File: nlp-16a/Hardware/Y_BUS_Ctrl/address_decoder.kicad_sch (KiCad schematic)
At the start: 20 parts, among them U41 CD74HC00, U42 CD74HC00

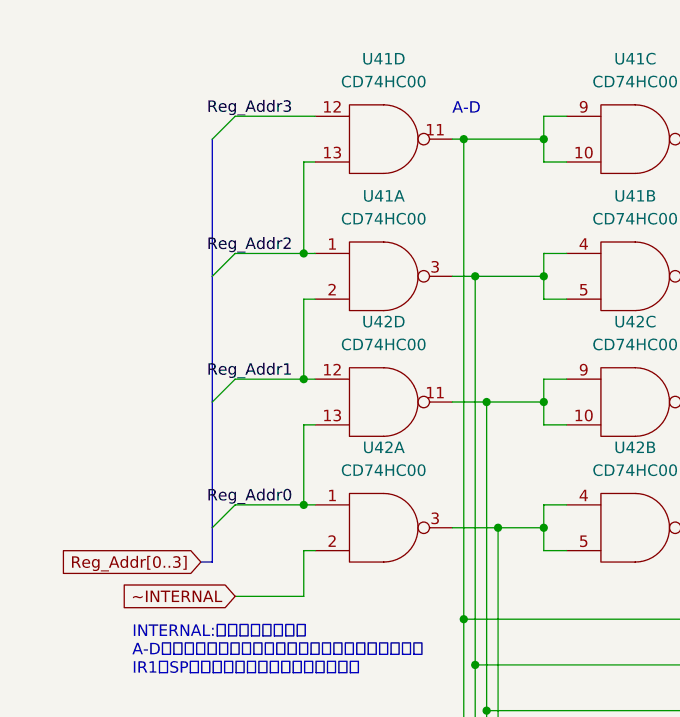
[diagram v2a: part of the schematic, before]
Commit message: Y BUS制御の基板をとりあえず描いた．ビアとかはまた後で
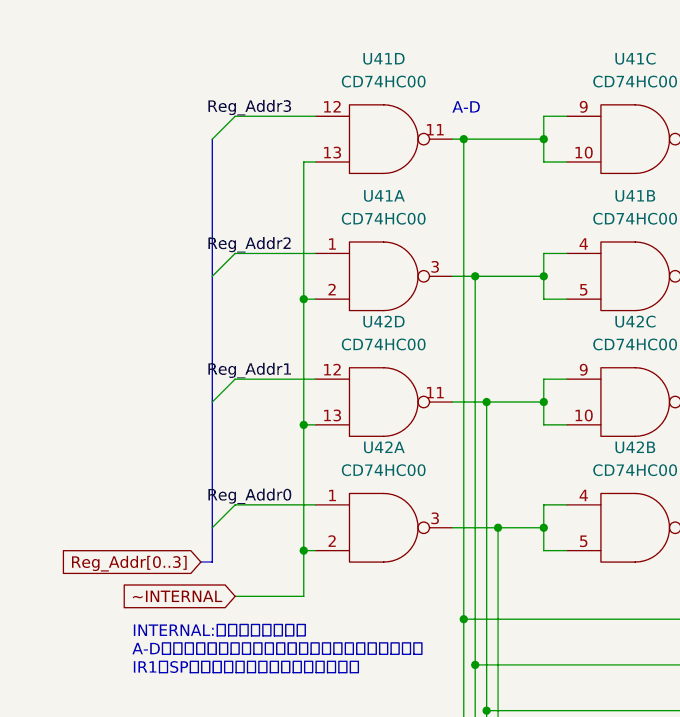
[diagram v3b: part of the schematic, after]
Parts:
- D17, D18, D19, D20, D21, D22, D23, D24, D25, D26, D27, D28, D29, D30, D31, D32: footprint (none) -> LED_THT:LED_D3.0mm
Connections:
- net Reg_Addr0: no longer U42.13
- net Reg_Addr1: no longer U41.2
- net Reg_Addr2: no longer U41.13
- net ~INTERNAL: now also U41.13, U41.2, U42.13
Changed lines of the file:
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@@
   (junction (at 142.24 83.82) (diameter 0) (color 0 0 0 0)
   )
+  (junction (at 34.29 68.58) (diameter 0) (color 0 0 0 0)
+  )
   (junction (at 115.57 114.3) (diameter 0) (color 0 0 0 0)
   )
@@
   (junction (at 252.73 48.26) (diameter 0) (color 0 0 0 0)
   )
-  (junction (at 34.29 49.53) (diameter 0) (color 0 0 0 0)
-  )
   (junction (at 172.72 157.48) (diameter 0) (color 0 0 0 0)
   )
@@
   (junction (at 256.54 81.28) (diameter 0) (color 0 0 0 0)
   )
-  (junction (at 34.29 35.56) (diameter 0) (color 0 0 0 0)
-  )
   (junction (at 161.29 78.74) (diameter 0) (color 0 0 0 0)
   )
@@
   (junction (at 60.96 66.04) (diameter 0) (color 0 0 0 0)
   )
-  (junction (at 34.29 63.5) (diameter 0) (color 0 0 0 0)
-  )
   (junction (at 252.73 142.24) (diameter 0) (color 0 0 0 0)
   )
@@
   (junction (at 276.86 41.91) (diameter 0) (color 0 0 0 0)
   )
+  (junction (at 34.29 40.64) (diameter 0) (color 0 0 0 0)
+  )
   (junction (at 55.88 91.44) (diameter 0) (color 0 0 0 0)
   )
@@
   (junction (at 82.55 88.9) (diameter 0) (color 0 0 0 0)
   )
+  (junction (at 34.29 54.61) (diameter 0) (color 0 0 0 0)
+  )
   (junction (at 229.87 142.24) (diameter 0) (color 0 0 0 0)
   )
@@
     (stroke (width 0) (type default) (color 0 0 0 0))
   )
-  (wire (pts (xy 34.29 35.56) (xy 35.56 35.56))
-    (stroke (width 0) (type default) (color 0 0 0 0))
-  )
   (wire (pts (xy 53.34 147.32) (xy 187.96 147.32))
     (stroke (width 0) (type default) (color 0 0 0 0))
@@
     (stroke (width 0) (type default) (color 0 0 0 0))
   )
-  (wire (pts (xy 34.29 54.61) (xy 34.29 63.5))
-    (stroke (width 0) (type default) (color 0 0 0 0))
-  )
   (wire (pts (xy 187.96 114.3) (xy 184.15 114.3))
     (stroke (width 0) (type default) (color 0 0 0 0))
@@
     (stroke (width 0) (type default) (color 0 0 0 0))
   )
+  (wire (pts (xy 34.29 40.64) (xy 34.29 54.61))
+    (stroke (width 0) (type default) (color 0 0 0 0))
+  )
   (wire (pts (xy 237.49 86.36) (xy 260.35 86.36))
     (stroke (width 0) (type default) (color 0 0 0 0))
@@
     (stroke (width 0) (type default) (color 0 0 0 0))
   )
+  (wire (pts (xy 34.29 25.4) (xy 34.29 40.64))
+    (stroke (width 0) (type default) (color 0 0 0 0))
+  )
   (wire (pts (xy 52.07 142.24) (xy 92.71 142.24))
     (stroke (width 0) (type default) (color 0 0 0 0))
@@
     (stroke (width 0) (type default) (color 0 0 0 0))
   )
-  (wire (pts (xy 34.29 49.53) (xy 35.56 49.53))
-    (stroke (width 0) (type default) (color 0 0 0 0))
-  )
   (wire (pts (xy 187.96 139.7) (xy 187.96 147.32))
     (stroke (width 0) (type default) (color 0 0 0 0))
@@
     (stroke (width 0) (type default) (color 0 0 0 0))
   )
-  (wire (pts (xy 34.29 25.4) (xy 34.29 35.56))
-    (stroke (width 0) (type default) (color 0 0 0 0))
-  )
-  (wire (pts (xy 26.67 63.5) (xy 34.29 63.5))
-    (stroke (width 0) (type default) (color 0 0 0 0))
-  )
   (wire (pts (xy 142.24 48.26) (xy 138.43 48.26))
     (stroke (width 0) (type default) (color 0 0 0 0))
@@
     (stroke (width 0) (type default) (color 0 0 0 0))
   )
-  (wire (pts (xy 34.29 63.5) (xy 35.56 63.5))
+  (wire (pts (xy 26.67 63.5) (xy 35.56 63.5))
     (stroke (width 0) (type default) (color 0 0 0 0))
   )
@@
     (stroke (width 0) (type default) (color 0 0 0 0))
   )
-  (wire (pts (xy 26.67 35.56) (xy 34.29 35.56))
+  (wire (pts (xy 26.67 35.56) (xy 35.56 35.56))
     (stroke (width 0) (type default) (color 0 0 0 0))
   )
@@
     (stroke (width 0) (type default) (color 0 0 0 0))
   )
+  (wire (pts (xy 34.29 54.61) (xy 34.29 68.58))
+    (stroke (width 0) (type default) (color 0 0 0 0))
+  )
   (wire (pts (xy 256.54 139.7) (xy 256.54 147.32))
     (stroke (width 0) (type default) (color 0 0 0 0))
@@
     (stroke (width 0) (type default) (color 0 0 0 0))
   )
-  (wire (pts (xy 34.29 40.64) (xy 34.29 49.53))
-    (stroke (width 0) (type default) (color 0 0 0 0))
-  )
   (wire (pts (xy 191.77 140.97) (xy 195.58 140.97))
     (stroke (width 0) (type default) (color 0 0 0 0))
@@
     (stroke (width 0) (type default) (color 0 0 0 0))
   )
-  (wire (pts (xy 26.67 49.53) (xy 34.29 49.53))
+  (wire (pts (xy 26.67 49.53) (xy 35.56 49.53))
     (stroke (width 0) (type default) (color 0 0 0 0))
   )
@@
     (property "Reference" "D29" (id 0) (at 193.04 116.84 0))
     (property "Value" "LED" (id 1) (at 189.23 116.84 0))
-    (property "Footprint" "" (id 2) (at 191.77 114.3 0)
+    (property "Footprint" "LED_THT:LED_D3.0mm" (id 2) (at 191.77 114.3 0)
       (effects (font (size 1.27 1.27)) hide)
     )
@@
     (property "Reference" "D26" (id 0) (at 124.46 116.84 0))
     (property "Value" "LED" (id 1) (at 120.65 116.84 0))
-    (property "Footprint" "" (id 2) (at 123.19 114.3 0)
+    (property "Footprint" "LED_THT:LED_D3.0mm" (id 2) (at 123.19 114.3 0)
       (effects (font (size 1.27 1.27)) hide)
     )
@@
     (property "Reference" "D22" (id 0) (at 215.9 50.8 0))
     (property "Value" "LED" (id 1) (at 212.09 50.8 0))
-    (property "Footprint" "" (id 2) (at 214.63 48.26 0)
+    (property "Footprint" "LED_THT:LED_D3.0mm" (id 2) (at 214.63 48.26 0)
       (effects (font (size 1.27 1.27)) hide)
     )
@@
     (property "Reference" "D24" (id 0) (at 261.62 50.8 0))
     (property "Value" "LED" (id 1) (at 257.81 50.8 0))
-    (property "Footprint" "" (id 2) (at 260.35 48.26 0)
+    (property "Footprint" "LED_THT:LED_D3.0mm" (id 2) (at 260.35 48.26 0)
       (effects (font (size 1.27 1.27)) hide)
     )
@@
     (property "Reference" "D18" (id 0) (at 124.46 50.8 0))
     (property "Value" "LED" (id 1) (at 120.65 50.8 0))
-    (property "Footprint" "" (id 2) (at 123.19 48.26 0)
+    (property "Footprint" "LED_THT:LED_D3.0mm" (id 2) (at 123.19 48.26 0)
       (effects (font (size 1.27 1.27)) hide)
     )
@@
     (property "Reference" "D17" (id 0) (at 101.6 50.8 0))
     (property "Value" "LED" (id 1) (at 97.79 50.8 0))
-    (property "Footprint" "" (id 2) (at 100.33 48.26 0)
+    (property "Footprint" "LED_THT:LED_D3.0mm" (id 2) (at 100.33 48.26 0)
       (effects (font (size 1.27 1.27)) hide)
     )
@@
     (property "Reference" "D31" (id 0) (at 238.76 116.84 0))
     (property "Value" "LED" (id 1) (at 234.95 116.84 0))
-    (property "Footprint" "" (id 2) (at 237.49 114.3 0)
+    (property "Footprint" "LED_THT:LED_D3.0mm" (id 2) (at 237.49 114.3 0)
       (effects (font (size 1.27 1.27)) hide)
     )
@@
     (property "Reference" "D32" (id 0) (at 261.62 116.84 0))
     (property "Value" "LED" (id 1) (at 257.81 116.84 0))
-    (property "Footprint" "" (id 2) (at 260.35 114.3 0)
+    (property "Footprint" "LED_THT:LED_D3.0mm" (id 2) (at 260.35 114.3 0)
       (effects (font (size 1.27 1.27)) hide)
     )
@@
     (property "Reference" "D19" (id 0) (at 147.32 50.8 0))
     (property "Value" "LED" (id 1) (at 143.51 50.8 0))
-    (property "Footprint" "" (id 2) (at 146.05 48.26 0)
+    (property "Footprint" "LED_THT:LED_D3.0mm" (id 2) (at 146.05 48.26 0)
       (effects (font (size 1.27 1.27)) hide)
     )
@@
     (property "Reference" "D25" (id 0) (at 101.6 116.84 0))
     (property "Value" "LED" (id 1) (at 97.79 116.84 0))
-    (property "Footprint" "" (id 2) (at 100.33 114.3 0)
+    (property "Footprint" "LED_THT:LED_D3.0mm" (id 2) (at 100.33 114.3 0)
       (effects (font (size 1.27 1.27)) hide)
     )
@@
     (property "Reference" "D23" (id 0) (at 238.76 50.8 0))
     (property "Value" "LED" (id 1) (at 234.95 50.8 0))
-    (property "Footprint" "" (id 2) (at 237.49 48.26 0)
+    (property "Footprint" "LED_THT:LED_D3.0mm" (id 2) (at 237.49 48.26 0)
       (effects (font (size 1.27 1.27)) hide)
     )
@@
     (property "Reference" "D27" (id 0) (at 147.32 116.84 0))
     (property "Value" "LED" (id 1) (at 143.51 116.84 0))
-    (property "Footprint" "" (id 2) (at 146.05 114.3 0)
+    (property "Footprint" "LED_THT:LED_D3.0mm" (id 2) (at 146.05 114.3 0)
       (effects (font (size 1.27 1.27)) hide)
     )
@@
     (property "Reference" "D21" (id 0) (at 193.04 50.8 0))
     (property "Value" "LED" (id 1) (at 189.23 50.8 0))
-    (property "Footprint" "" (id 2) (at 191.77 48.26 0)
+    (property "Footprint" "LED_THT:LED_D3.0mm" (id 2) (at 191.77 48.26 0)
       (effects (font (size 1.27 1.27)) hide)
     )
@@
     (property "Reference" "D28" (id 0) (at 170.18 116.84 0))
     (property "Value" "LED" (id 1) (at 166.37 116.84 0))
-    (property "Footprint" "" (id 2) (at 168.91 114.3 0)
+    (property "Footprint" "LED_THT:LED_D3.0mm" (id 2) (at 168.91 114.3 0)
       (effects (font (size 1.27 1.27)) hide)
     )
@@
     (property "Reference" "D30" (id 0) (at 215.9 116.84 0))
     (property "Value" "LED" (id 1) (at 212.09 116.84 0))
-    (property "Footprint" "" (id 2) (at 214.63 114.3 0)
+    (property "Footprint" "LED_THT:LED_D3.0mm" (id 2) (at 214.63 114.3 0)
       (effects (font (size 1.27 1.27)) hide)
     )
@@
     (property "Reference" "D20" (id 0) (at 170.18 50.8 0))
     (property "Value" "LED" (id 1) (at 166.37 50.8 0))
-    (property "Footprint" "" (id 2) (at 168.91 48.26 0)
-      (effects (font (size 1.27 1.27)) hide)
-    )
+    (property "Footprint" "LED_THT:LED_D3.0mm" (id 2) (at 168.91 48.26 0)
+      (effects (font (size 1.27 1.27)) hide)
+    )

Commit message: Y BUS制御 更新
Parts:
- added U45: CD74HC00, Package_DIP:DIP-14_W7.62mm, symbol CD74HCXX:CD74HC00
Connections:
- net GND: now also U45.7 (GND), U45.7 (GND), U45.7 (GND), U45.7 (GND)
- net Reg_Addr0: now also U45.9; no longer U42.1
- net Reg_Addr1: now also U45.12; no longer U42.12
- net Reg_Addr2: now also U45.4; no longer U41.1
- net Reg_Addr3: now also U45.1; no longer U41.12
- net VCC: now also U45.10, U45.13, U45.14 (VCC), U45.14 (VCC), U45.14 (VCC), U45.14 (VCC), U45.2, U45.5
- new net: U41.1, U45.6
- new net: U42.12, U45.11
- new net: U42.1, U45.8
- new net: U41.12, U45.3
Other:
- moved on the sheet: U41A, U41D, U42A, U42D
